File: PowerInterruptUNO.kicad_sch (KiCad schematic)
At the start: 4 parts, among them J1 Power, J2 Digital/PWM, J3 Analog, J4 Digital/PWM

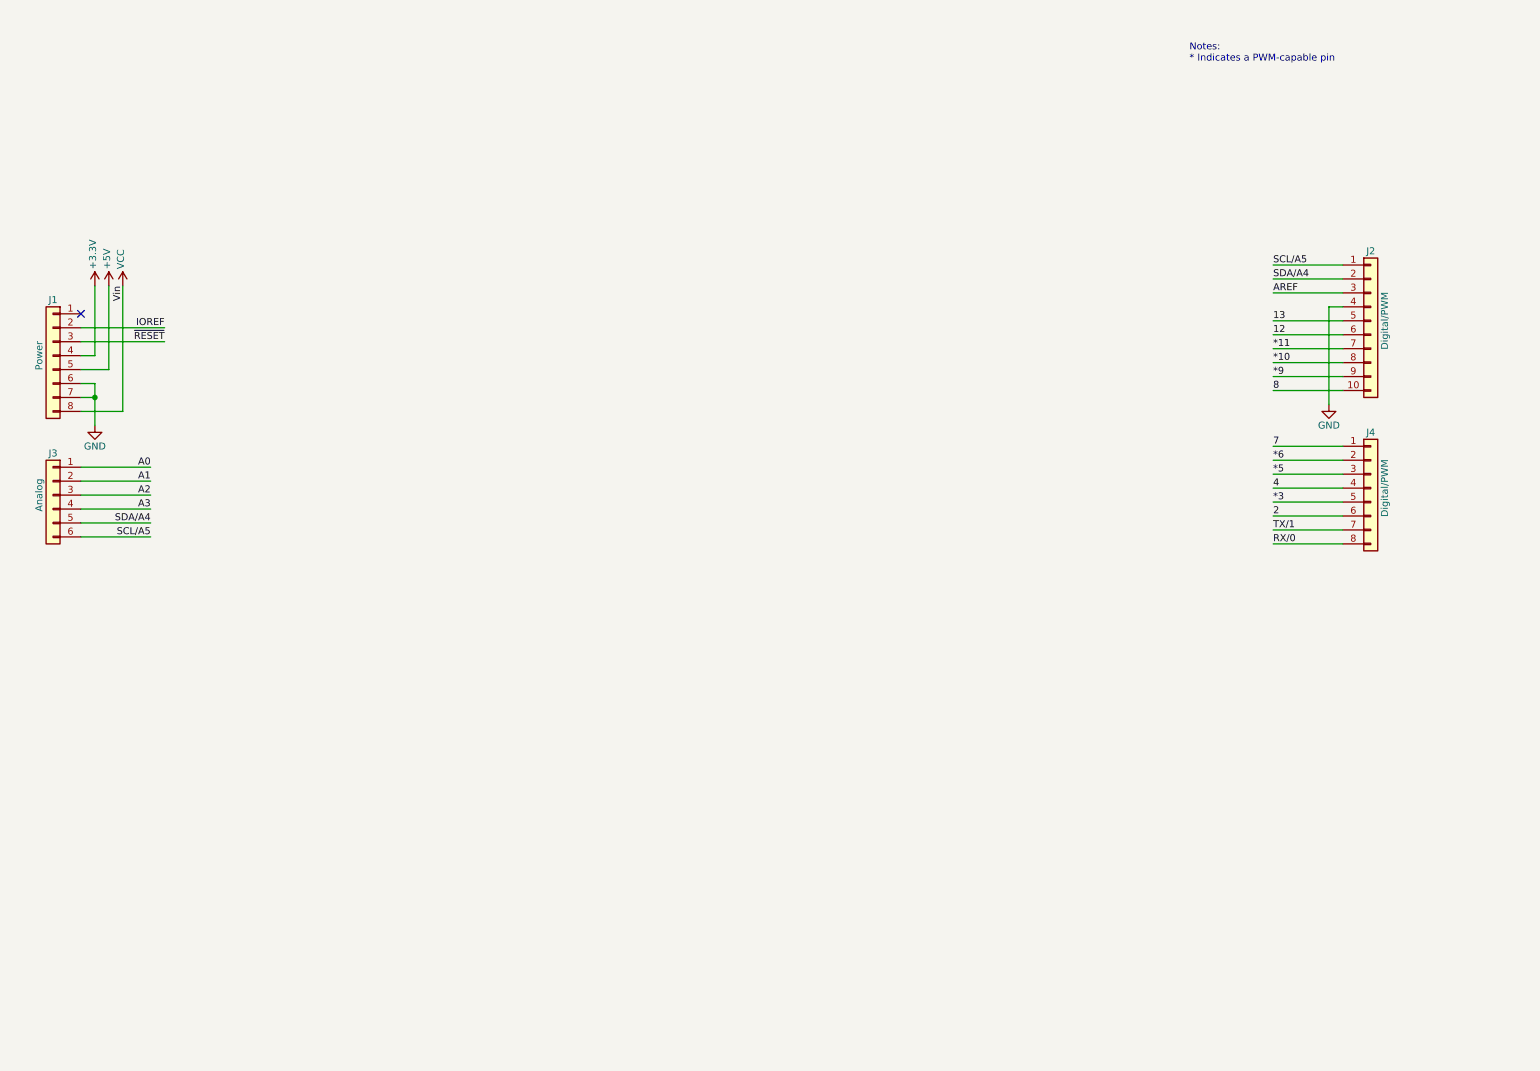
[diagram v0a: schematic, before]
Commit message: Rough out schematic for power in. Current limit. Switched power to terminal, USBA, USBC, RJ12 SPI Controler. Inputs terminals for interupt and ADC.
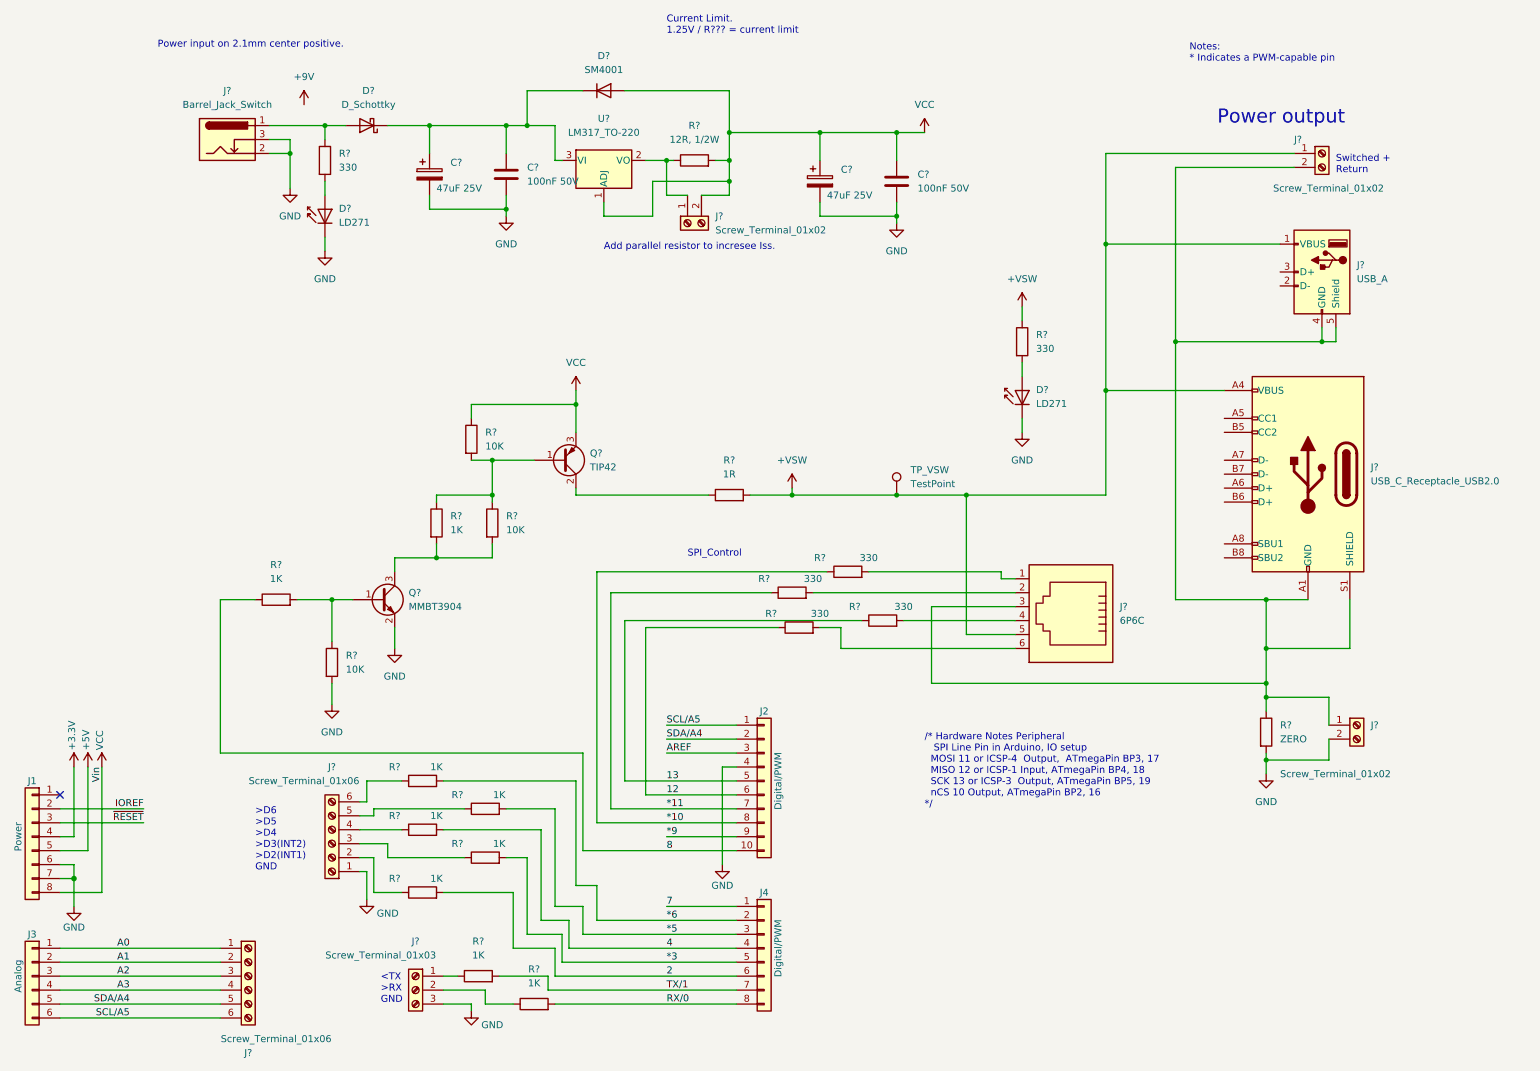
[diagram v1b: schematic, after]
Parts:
- added C? (x2): 100nF 50V, Capacitor_SMD:C_0603_1608Metric_Pad1.08x0.95mm_HandSolder, symbol Device:C
- added C? (x2): 47uF 25V, Capacitor_SMD:CP_Elec_6.3x5.3, symbol Device:C_Polarized
- added D?: D_Schottky, symbol Device:D_Schottky
- added D? (x2): LD271, LED_THT:LED_D5.0mm_IRGrey, symbol LED:LD271
- added D?: SM4001, Diode_SMD:D_MELF, symbol Diode:SM4001
- added J? (x2): Screw_Terminal_01x02, TerminalBlock_TE-Connectivity:TerminalBlock_TE_282834-2_1x02_P2.54mm_Horizontal, symbol Connector:Screw_Terminal_01x02
- added J?: USB_A, symbol Connector:USB_A
- added J? (x2): Screw_Terminal_01x06, symbol Connector:Screw_Terminal_01x06
- added J?: Barrel_Jack_Switch, symbol Connector:Barrel_Jack_Switch
- added J?: Screw_Terminal_01x03, symbol Connector:Screw_Terminal_01x03
- added J?: USB_C_Receptacle_USB2.0, symbol Connector:USB_C_Receptacle_USB2.0
- added J?: Screw_Terminal_01x02, symbol Connector:Screw_Terminal_01x02
- added J?: 6P6C, symbol Connector:6P6C
- added Q?: MMBT3904, Package_TO_SOT_SMD:SOT-23, symbol Transistor_BJT:MMBT3904
- added Q?: TIP42, Package_TO_SOT_THT:TO-220-3_Vertical, symbol Transistor_BJT:TIP42
- added R? (x3): 10K, Resistor_SMD:R_0603_1608Metric_Pad0.98x0.95mm_HandSolder, symbol Device:R
- added R?: 12R, 1/2W, Resistor_THT:R_Axial_DIN0414_L11.9mm_D4.5mm_P25.40mm_Horizontal, symbol Device:R
- added R? (x6): 330, Resistor_SMD:R_0603_1608Metric_Pad0.98x0.95mm_HandSolder, symbol Device:R
- added R?: ZERO, Resistor_SMD:R_0603_1608Metric_Pad0.98x0.95mm_HandSolder, symbol Device:R
- added R? (x9): 1K, Resistor_SMD:R_0603_1608Metric_Pad0.98x0.95mm_HandSolder, symbol Device:R
- added R?: 1R, Resistor_SMD:R_0603_1608Metric_Pad0.98x0.95mm_HandSolder, symbol Device:R
- added TP_VSW: TestPoint, TestPoint:TestPoint_Loop_D2.50mm_Drill1.85mm, symbol Connector:TestPoint
- added U?: LM317_TO-220, Package_TO_SOT_THT:TO-220-3_Vertical, symbol Regulator_Linear:LM317_TO-220
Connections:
- net *10: now also R?.1
- net *11: now also R?.1
- net *3: now also R?.2
- net *5: now also R?.2
- net *6: now also R?.2
- net 12: now also R?.1
- net 13: now also R?.1
- net 2: now also R?.2
- net 4: now also R?.2
- net 8: now also R?.1
- net A0: now also J?.1 (Pin_1)
- net A1: now also J?.2 (Pin_2)
- net A2: now also J?.3 (Pin_3)
- net A3: now also J?.4 (Pin_4)
- net GND: now also C?.2, C?.2, C?.2, C?.2, D?.1 (K), D?.1 (K), J?.1 (Pin_1), J?.2, J?.2 (Pin_2), J?.3, J?.3 (Pin_3), Q?.2 (E), R?.2, R?.2
- net RX/0: now also R?.2
- net SCL/A5: now also J?.6 (Pin_6)
- net SDA/A4: now also J?.5 (Pin_5)
- net TX/1: now also R?.2
- net VCC: now also C?.1, C?.1, D?.2 (A), J?.2 (Pin_2), Q?.3 (E), R?.1, R?.2, U?.1 (ADJ)
- new net: J?.1 (Pin_1), J?.2 (Pin_2), J?.3, J?.4 (GND), J?.5 (Shield), J?.A1 (GND), J?.A12 (GND), J?.B1 (GND), J?.B12 (GND), J?.S1 (SHIELD), R?.1
- new net: Q?.1 (B), R?.1, R?.1, R?.2
- new net: C?.1, C?.1, D?.1 (K), D?.1 (K), U?.3 (VI)
- new net: J?.1 (Pin_1), R?.1, U?.2 (VO)
- new net: J?.4, R?.2
- new net: D?.2 (A), J?.1, R?.1
- new net: D?.2 (A), R?.2 (x2)
- new net: Q?.1 (B), R?.1, R?.2
- new net: J?.5 (Pin_5), R?.1
- new net: J?.1 (Pin_1), R?.1
- new net: J?.4 (Pin_4), R?.1
- new net: J?.2 (Pin_2), R?.1 (x2)
- new net: Q?.3 (C), R?.2, R?.2
- new net: J?.2, R?.2
- new net: J?.3 (Pin_3), R?.1
- new net: J?.6 (Pin_6), R?.1
- new net: J?.1, R?.2
- new net: Q?.2 (C), R?.1
- new net: J?.6, R?.2
- new net +VSW: J?.1 (Pin_1), J?.1 (VBUS), J?.5, J?.A4 (VBUS), J?.A9 (VBUS), J?.B4 (VBUS), J?.B9 (VBUS), R?.1, R?.2, TP_VSW.1
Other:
- note added: "/* Hardware Notes Peripheral SPI Line Pin in Arduino, IO setup MOSI 11 or ICSP-4 Output, ATmegaPin BP3, 17 MISO 12 or ICSP-1 Input, ATmegaPin BP4, 18 SCK 13 or ICSP-3 Output, ATmegaPin BP5, 19 nCS 10 Output, ATmegaPin BP2, 16 */"
- note added: "<TX >RX GND"
- note added: ">D6 >D5 >D4 >D3(INT2) >D2(INT1) GND"
- note added: "Add parallel resistor to incresee Iss."
- note added: "Current Limit. 1.25V / R??? = current limit"
- note added: "Power input on 2.1mm center positive."
- note added: "Power output"
- note added: "SPI_Control"
- note added: "Switched + Return"
- moved on the sheet: J1, J2, J3, J4

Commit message: Annote schematic.
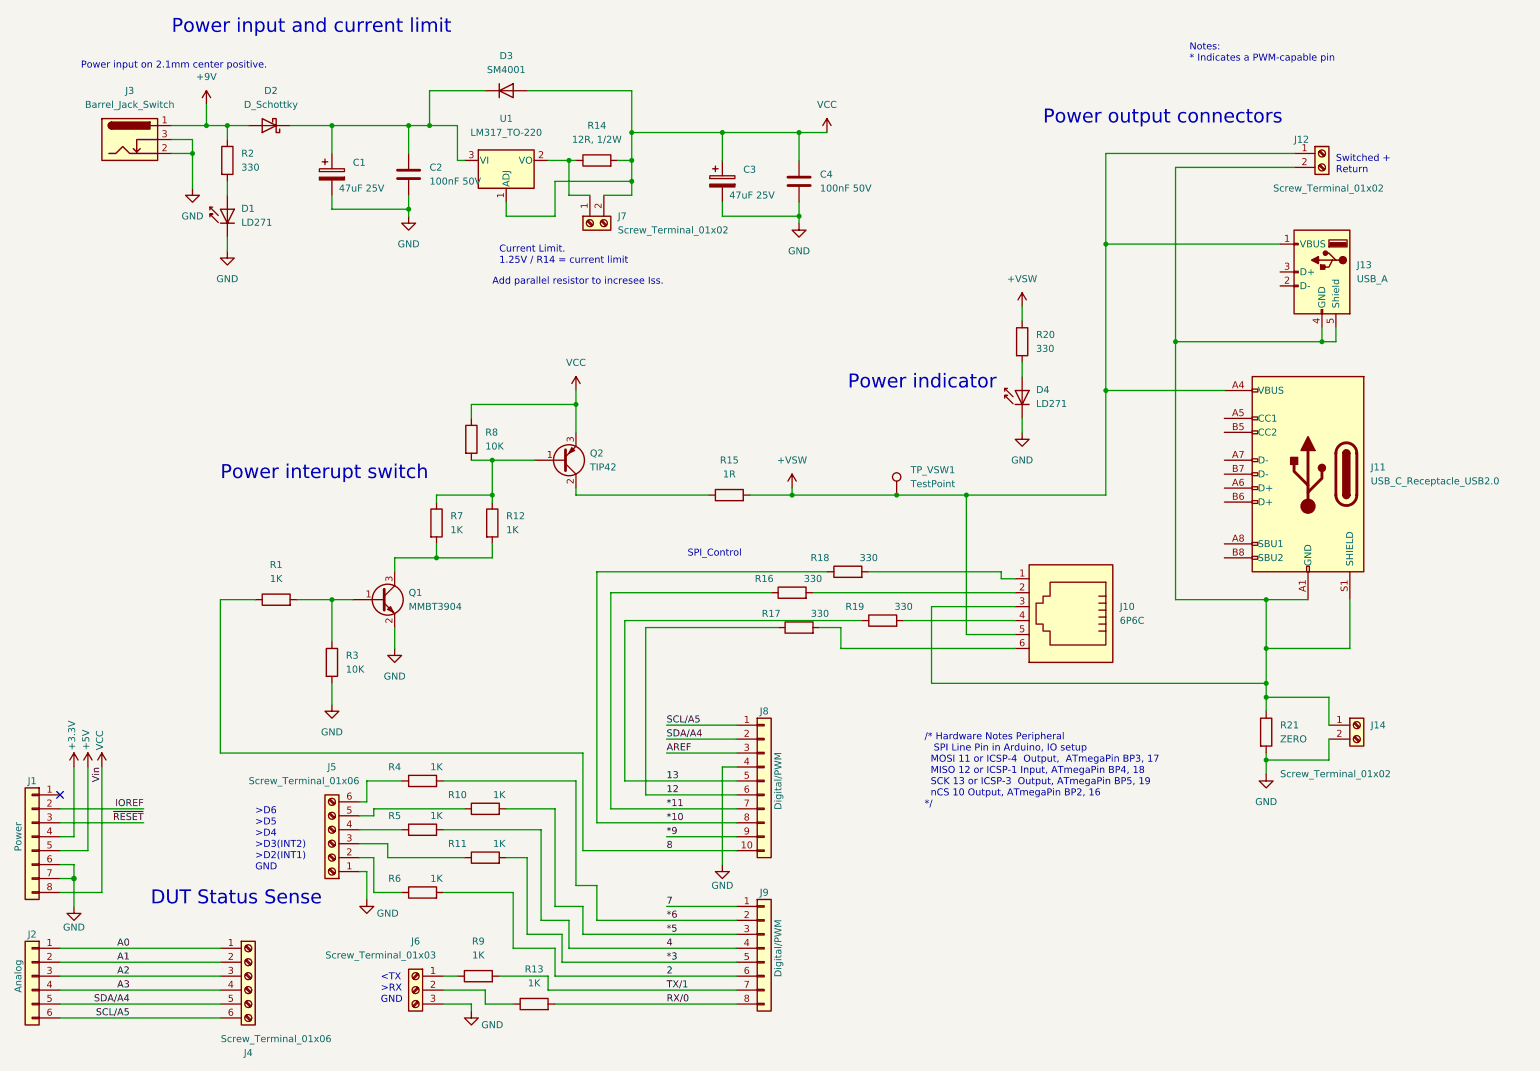
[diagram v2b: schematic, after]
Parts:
- R12: renamed from R?; value 10K -> 1K
- gave numbers to parts that had none: 41
- renumbered J3 to J2, J2 to J8, J4 to J9, TP_VSW to TP_VSW1
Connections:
- net +9V: now also D2.2 (A), J3.1, R2.1
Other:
- note added: "Current Limit. 1.25V / R14 = current limit"
- note added: "DUT Status Sense"
- note added: "Power indicator"
- note added: "Power input and current limit"
- note added: "Power interupt switch"
- note added: "Power output connectors"
- note removed: "Current Limit. 1.25V / R??? = current limit"
- note removed: "Power output"
- moved on the sheet: C1, C2, C3, C4, D1, D2, D3, J3, J7, R14, R2, U1

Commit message: Clear electrical rules check on schematic.
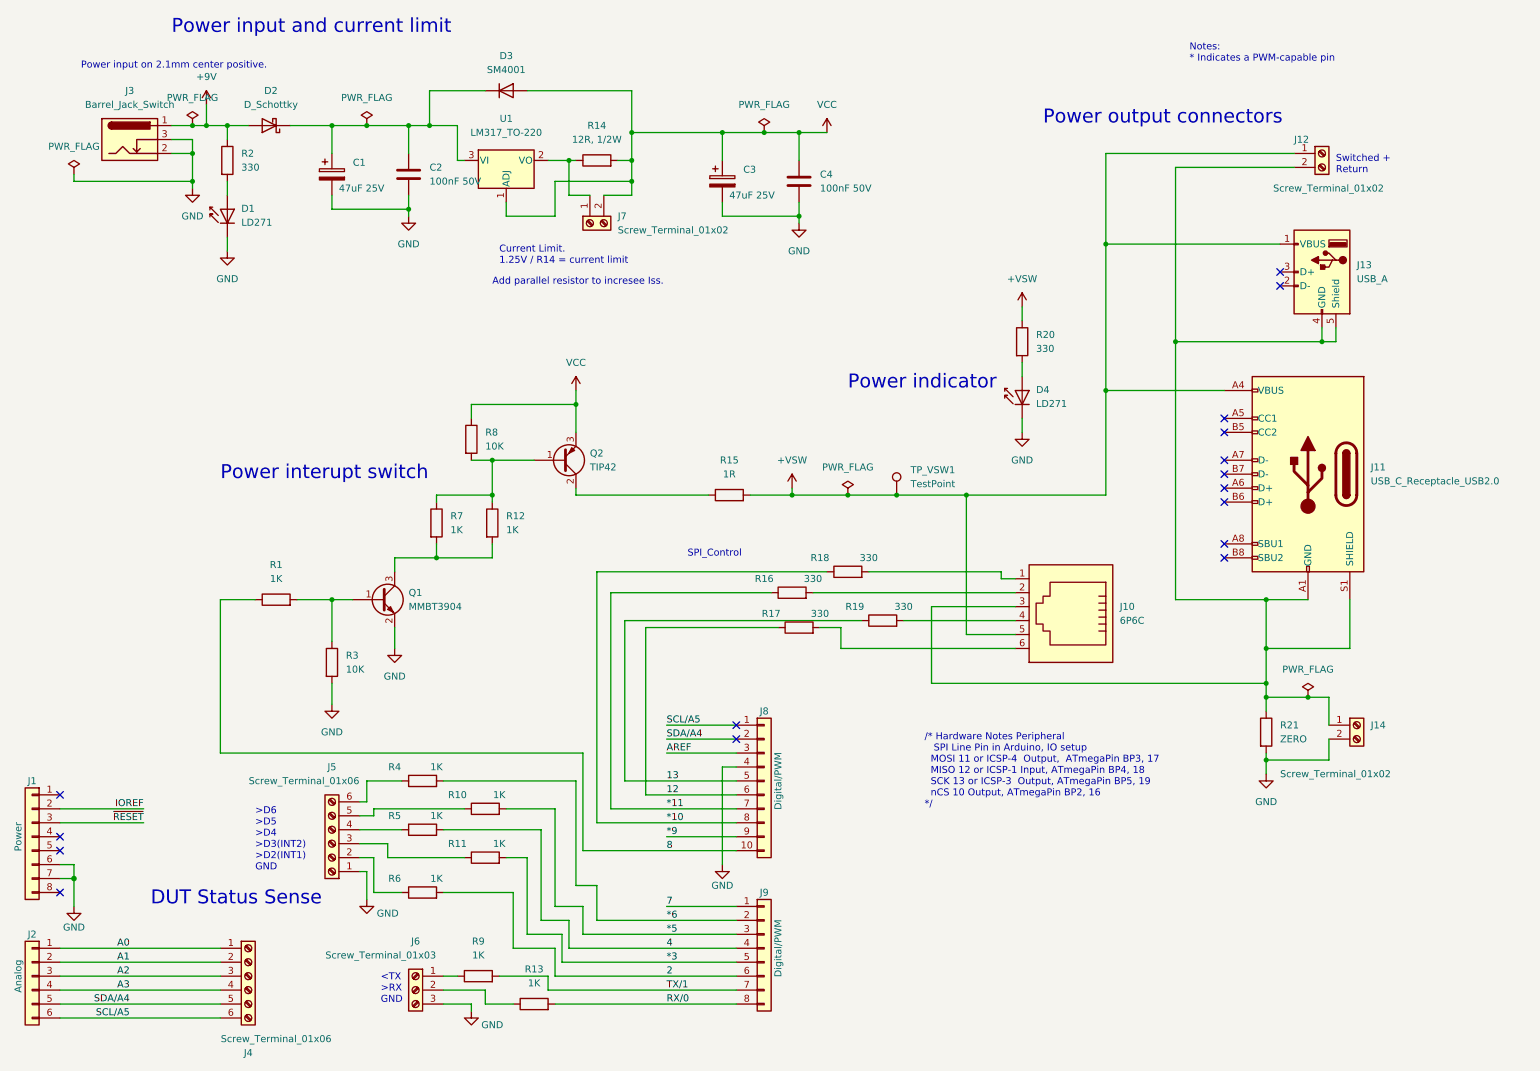
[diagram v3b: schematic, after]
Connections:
- net VCC: no longer J1.8 (Pin_8)
- net +3V3: no longer names the net of J1.4 (Pin_4)
- net +5V: no longer names the net of J1.5 (Pin_5)
- no-connect marks 1 -> 16
